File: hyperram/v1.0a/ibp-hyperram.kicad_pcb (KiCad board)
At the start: 2 copper layers, 18 x 42 mm, 6 parts, among them J2 PMOD, J4 PMOD, U1 S70KL1281

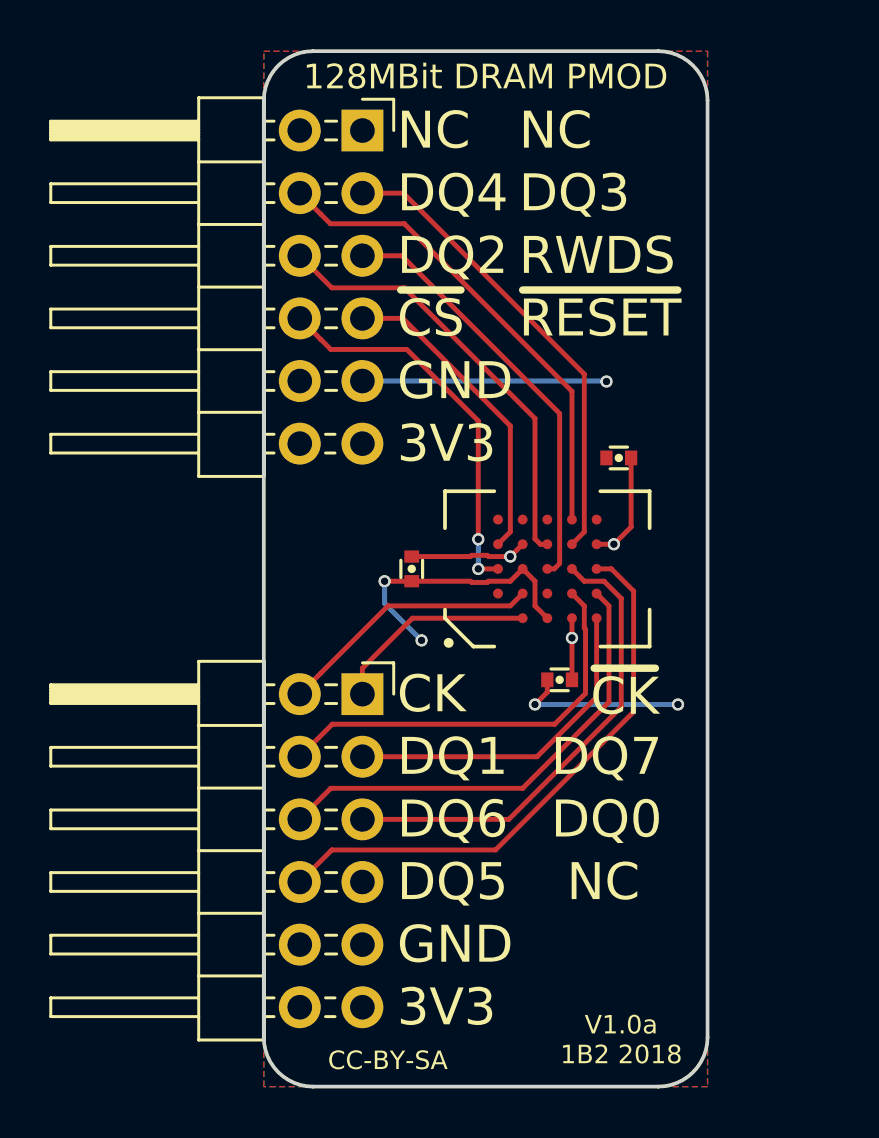
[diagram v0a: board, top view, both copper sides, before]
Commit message: Corrected silkscreen legend, roundrect pads.
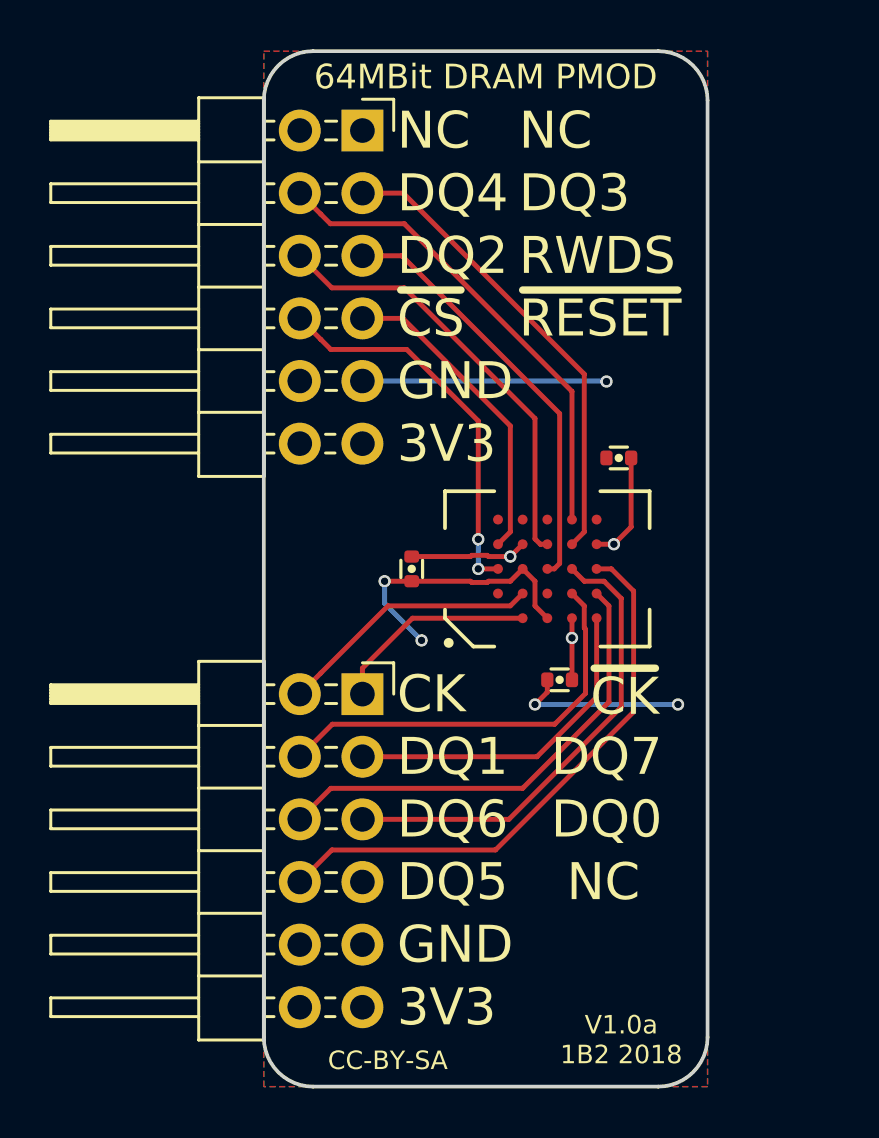
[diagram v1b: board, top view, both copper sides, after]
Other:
- board text added: "64MBit DRAM PMOD"
- board text removed: "128MBit DRAM PMOD"
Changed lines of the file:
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@@
-(kicad_pcb (version 20171130) (host pcbnew 5.0.0-rc2-dev-unknown-1ac905d~64~ubuntu16.04.1)
+(kicad_pcb (version 20171130) (host pcbnew 5.0.0-rc2-dev-unknown-5a90858~64~ubuntu16.04.1)
   (general
     (thickness 0.8)
@@
     (mod_text_size 1 1)
     (mod_text_width 0.15)
-    (pad_size 1.7 1.7)
-    (pad_drill 1)
+    (pad_size 0.5 0.6)
+    (pad_drill 0)
     (pad_to_mask_clearance 0.05)
     (aux_axis_origin 0 0)
@@
     (fp_line (start -0.35 -0.44) (end 0.35 -0.44) (layer F.SilkS) (width 0.13))
     (fp_line (start 0.35 0.44) (end -0.35 0.44) (layer F.SilkS) (width 0.13))
-    (pad 1 smd rect (at -0.5 0 180) (size 0.5 0.6) (layers F.Cu F.Paste F.Mask)
-      (net 3 +3V3))
-    (pad 2 smd rect (at 0.5 0 180) (size 0.5 0.6) (layers F.Cu F.Paste F.Mask)
+    (pad 1 smd roundrect (at -0.5 0 180) (size 0.5 0.6) (layers F.Cu F.Paste F.Mask) (roundrect_rratio 0.25)
+      (net 3 +3V3))
+    (pad 2 smd roundrect (at 0.5 0 180) (size 0.5 0.6) (layers F.Cu F.Paste F.Mask) (roundrect_rratio 0.25)
       (net 1 GND))
     (model ${KISYS3DMOD}/Capacitor_SMD.3dshapes/C_0402_1005Metric.step
@@
     (fp_line (start -0.95 -0.5) (end 0.95 -0.5) (layer F.CrtYd) (width 0.05))
     (fp_circle (center 0 0) (end 0 -0.085) (layer F.SilkS) (width 0.17))
-    (pad 2 smd rect (at 0.5 0 180) (size 0.5 0.6) (layers F.Cu F.Paste F.Mask)
-      (net 1 GND))
-    (pad 1 smd rect (at -0.5 0 180) (size 0.5 0.6) (layers F.Cu F.Paste F.Mask)
+    (pad 2 smd roundrect (at 0.5 0 180) (size 0.5 0.6) (layers F.Cu F.Paste F.Mask) (roundrect_rratio 0.25)
+      (net 1 GND))
+    (pad 1 smd roundrect (at -0.5 0 180) (size 0.5 0.6) (layers F.Cu F.Paste F.Mask) (roundrect_rratio 0.25)
       (net 3 +3V3))
     (model Capacitors_SMD.3dshapes/C_0402.wrl
@@
     (fp_line (start -0.35 -0.44) (end 0.35 -0.44) (layer F.SilkS) (width 0.13))
     (fp_line (start 0.35 0.44) (end -0.35 0.44) (layer F.SilkS) (width 0.13))
-    (pad 1 smd rect (at -0.5 0 270) (size 0.5 0.6) (layers F.Cu F.Paste F.Mask)
-      (net 3 +3V3))
-    (pad 2 smd rect (at 0.5 0 270) (size 0.5 0.6) (layers F.Cu F.Paste F.Mask)
+    (pad 1 smd roundrect (at -0.5 0 270) (size 0.5 0.6) (layers F.Cu F.Paste F.Mask) (roundrect_rratio 0.25)
+      (net 3 +3V3))
+    (pad 2 smd roundrect (at 0.5 0 270) (size 0.5 0.6) (layers F.Cu F.Paste F.Mask) (roundrect_rratio 0.25)
       (net 1 GND))
     (model ${KISYS3DMOD}/Capacitor_SMD.3dshapes/C_0402_1005Metric.step
@@
     (effects (font (size 0.75 0.75) (thickness 0.1875)) (justify mirror))
   )
-  (gr_text "128MBit DRAM PMOD" (at 49 24.045) (layer B.SilkS)
+  (gr_text "64MBit DRAM PMOD" (at 49 24.045) (layer B.SilkS)
     (effects (font (size 1 1) (thickness 0.25)) (justify mirror))
   )
-  (gr_text "128MBit DRAM PMOD" (at 49 24.045) (layer F.SilkS)
+  (gr_text "64MBit DRAM PMOD" (at 49 24.045) (layer F.SilkS)
     (effects (font (size 1 1) (thickness 0.25)))
   )

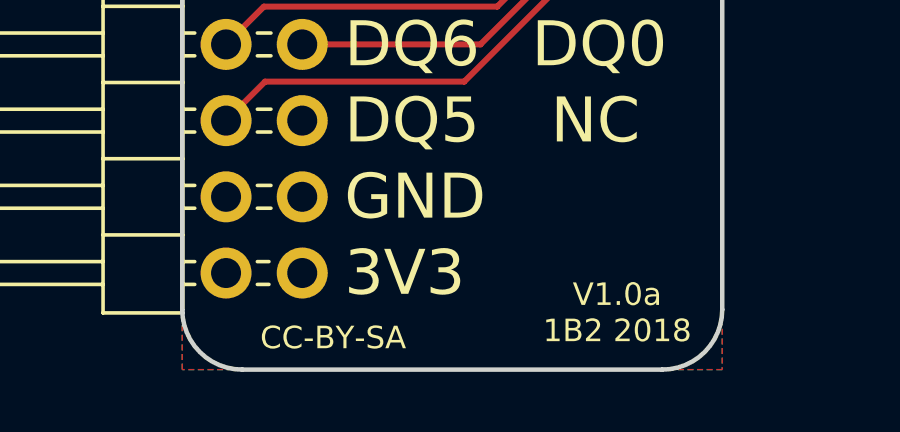
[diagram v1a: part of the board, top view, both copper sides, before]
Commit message: Spelled out 1BitSquared copyright.
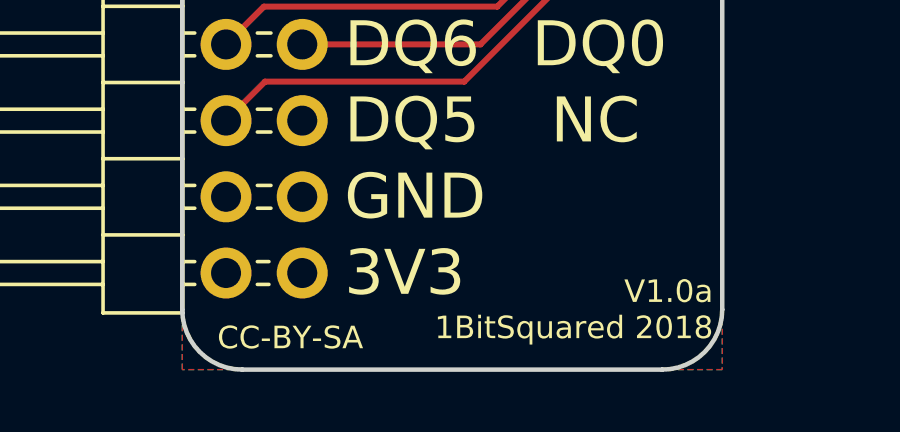
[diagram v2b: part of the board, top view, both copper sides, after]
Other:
- board text added: "V1.0a 1BitSquared 2018"
- board text removed: "V1.0a 1B2 2018"
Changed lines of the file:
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@@
-(kicad_pcb (version 20171130) (host pcbnew 5.0.0-rc2-dev-unknown-5a90858~64~ubuntu16.04.1)
+(kicad_pcb (version 20171130) (host pcbnew 5.0.0-fee4fd1~66~ubuntu18.04.1)
   (general
     (thickness 0.8)
@@
       (hpglpennumber 1)
       (hpglpenspeed 20)
-      (hpglpendiameter 15)
+      (hpglpendiameter 15.000000)
       (psnegative false)
       (psa4output false)
@@
       (drillshape 0)
       (scaleselection 1)
-      (outputdirectory gerber))
+      (outputdirectory "gerber"))
   )
   (net 0 "")
@@
     )
   )
+  (gr_text "V1.0a\n1BitSquared 2018" (at 57.6 63) (layer B.SilkS)
+    (effects (font (size 0.75 0.75) (thickness 0.1875)) (justify left mirror))
+  )
   (gr_text NC (at 52.285 56.7) (layer F.SilkS)
     (effects (font (size 1.5 1.5) (thickness 0.3)) (justify left))
@@
     (effects (font (size 1.5 1.5) (thickness 0.3)) (justify left))
   )
-  (gr_text CC-BY-SA (at 44.93 63.94) (layer B.SilkS)
+  (gr_text CC-BY-SA (at 43.8 63.94) (layer B.SilkS)
     (effects (font (size 0.75 0.75) (thickness 0.1875)) (justify mirror))
   )
-  (gr_text CC-BY-SA (at 45.03 63.94) (layer F.SilkS)
+  (gr_text CC-BY-SA (at 43.6 63.94) (layer F.SilkS)
     (effects (font (size 0.75 0.75) (thickness 0.1875)))
   )
-  (gr_text "V1.0a\n1B2 2018" (at 54.5 63.1) (layer F.SilkS)
-    (effects (font (size 0.75 0.75) (thickness 0.1875)))
-  )
-  (gr_text "V1.0a\n1B2 2018" (at 54.5 63.1) (layer B.SilkS)
-    (effects (font (size 0.75 0.75) (thickness 0.1875)) (justify mirror))
+  (gr_text "V1.0a\n1BitSquared 2018" (at 57.7 63) (layer F.SilkS)
+    (effects (font (size 0.75 0.75) (thickness 0.1875)) (justify right))
   )
   (gr_text "64MBit DRAM PMOD" (at 49 24.045) (layer B.SilkS)

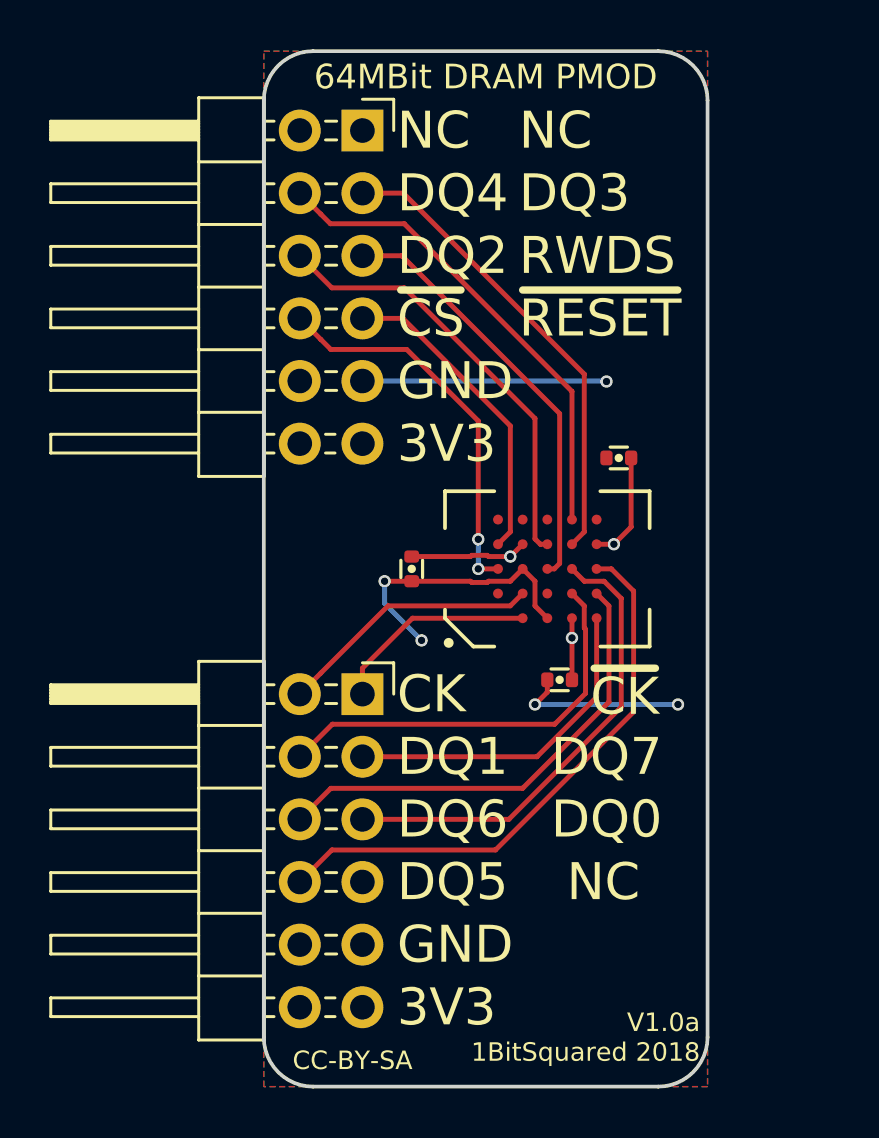
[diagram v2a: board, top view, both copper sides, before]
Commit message: Extended board outline to extend under the pin headers.
This makes assembly and alignment of the PMOD pin headers easier.
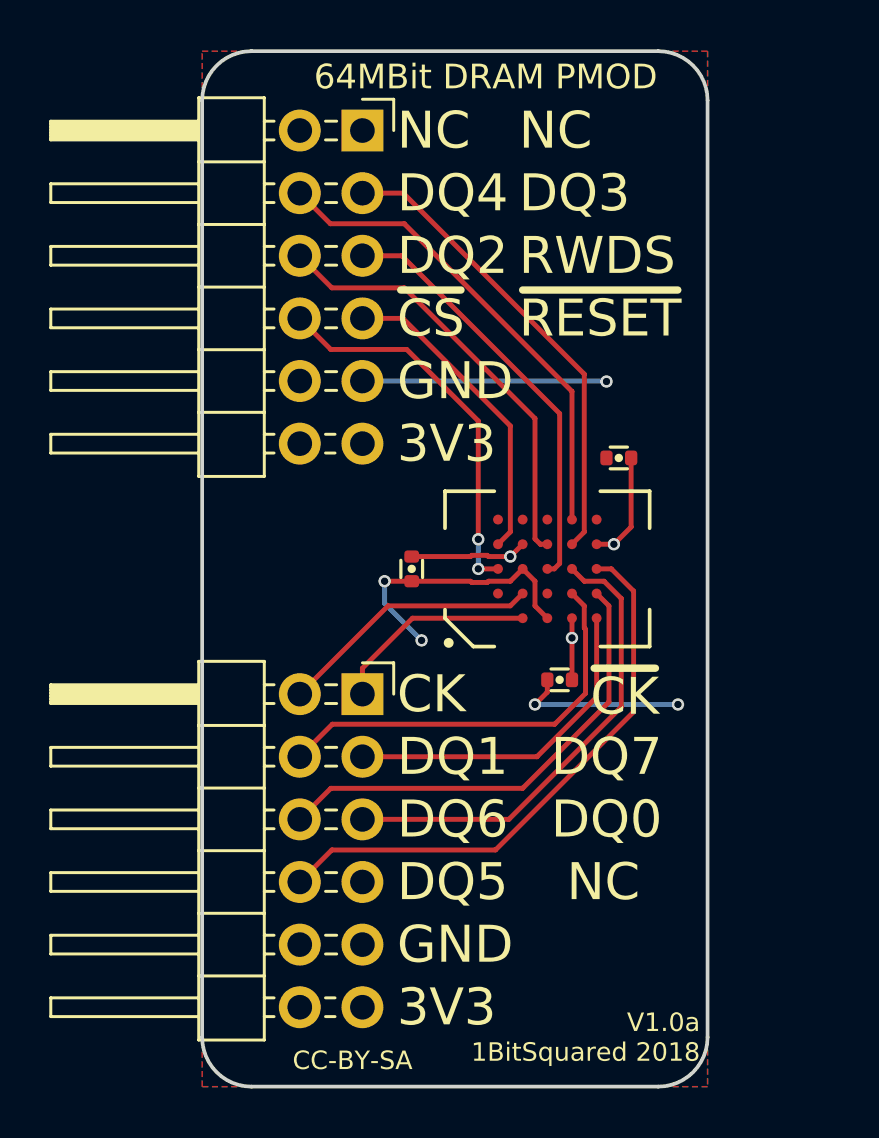
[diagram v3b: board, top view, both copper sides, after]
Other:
- board size 18 x 42 mm -> 20.5 x 42 mm
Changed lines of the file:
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@@
     (thickness 0.8)
     (drawings 54)
-    (tracks 105)
+    (tracks 102)
     (zones 0)
     (modules 6)
@@
   )
   (gr_arc (start 56 25) (end 58 25) (angle -90) (layer Edge.Cuts) (width 0.15))
-  (gr_arc (start 42 25) (end 42 23) (angle -90) (layer Edge.Cuts) (width 0.15))
-  (gr_arc (start 42 63) (end 40 63) (angle -90) (layer Edge.Cuts) (width 0.15))
+  (gr_arc (start 39.5 25) (end 39.5 23) (angle -90) (layer Edge.Cuts) (width 0.15))
+  (gr_arc (start 39.5 63) (end 37.5 63) (angle -90) (layer Edge.Cuts) (width 0.15))
   (gr_arc (start 56 63) (end 56 65) (angle -90) (layer Edge.Cuts) (width 0.15))
   (gr_line (start 58 25) (end 58 63) (layer Edge.Cuts) (width 0.15))
-  (gr_line (start 42 23) (end 56 23) (layer Edge.Cuts) (width 0.15))
-  (gr_line (start 40 63) (end 40 25) (layer Edge.Cuts) (width 0.15))
-  (gr_line (start 56 65) (end 42 65) (layer Edge.Cuts) (width 0.15))
+  (gr_line (start 39.5 23) (end 56 23) (layer Edge.Cuts) (width 0.15))
+  (gr_line (start 37.5 63) (end 37.5 25) (layer Edge.Cuts) (width 0.15))
+  (gr_line (start 56 65) (end 39.5 65) (layer Edge.Cuts) (width 0.15))
   (segment (start 51.5 46) (end 51 45.5) (width 0.2) (layer F.Cu) (net 1))
   (segment (start 51 44.5) (end 50.5 44) (width 0.2) (layer F.Cu) (net 1))
@@
   (segment (start 53.5 49.2) (end 53.5 46) (width 0.2) (layer F.Cu) (net 4))
   (segment (start 51.08 51.62) (end 53.5 49.2) (width 0.2) (layer F.Cu) (net 4))
-  (segment (start 42.309999 48.230001) (end 41.46 49.08) (width 0.2) (layer F.Cu) (net 6))
-  (segment (start 45.039999 45.500001) (end 42.309999 48.230001) (width 0.2) (layer F.Cu) (net 6))
-  (segment (start 49.999999 45.500001) (end 45.039999 45.500001) (width 0.2) (layer F.Cu) (net 6))
-  (segment (start 50.5 45) (end 49.999999 45.500001) (width 0.2) (layer F.Cu) (net 6))
+  (segment (start 49.999999 45.500001) (end 50.5 45) (width 0.2) (layer F.Cu) (net 6))
+  (segment (start 41.46 49.08) (end 45.039999 45.500001) (width 0.2) (layer F.Cu) (net 6))
+  (segment (start 45.039999 45.500001) (end 49.999999 45.500001) (width 0.2) (layer F.Cu) (net 6))
   (segment (start 53 45.5) (end 52.5 45) (width 0.2) (layer F.Cu) (net 8))
   (segment (start 53 46.4) (end 53 45.5) (width 0.2) (layer F.Cu) (net 8))
@@
   (via (at 48.7 42.8) (size 0.5) (drill 0.3) (layers F.Cu B.Cu) (net 10))
   (segment (start 48.7 44) (end 48.7 42.8) (width 0.2) (layer B.Cu) (net 10))
-  (segment (start 48.7 42.8) (end 48.7 38) (width 0.2) (layer F.Cu) (net 10))
-  (segment (start 42.309999 34.689999) (end 41.46 33.84) (width 0.2) (layer F.Cu) (net 10))
-  (segment (start 42.72 35.1) (end 42.309999 34.689999) (width 0.2) (layer F.Cu) (net 10))
-  (segment (start 48.7 38) (end 45.8 35.1) (width 0.2) (layer F.Cu) (net 10))
-  (segment (start 45.8 35.1) (end 42.72 35.1) (width 0.2) (layer F.Cu) (net 10))
+  (segment (start 48.7 38) (end 48.7 42.8) (width 0.2) (layer F.Cu) (net 10))
+  (segment (start 45.8 35.1) (end 48.7 38) (width 0.2) (layer F.Cu) (net 10))
+  (segment (start 41.46 33.84) (end 42.72 35.1) (width 0.2) (layer F.Cu) (net 10))
+  (segment (start 42.72 35.1) (end 45.8 35.1) (width 0.2) (layer F.Cu) (net 10))
   (segment (start 51.782842 44) (end 52 43.782842) (width 0.2) (layer F.Cu) (net 11))
   (segment (start 51.5 44) (end 51.782842 44) (width 0.2) (layer F.Cu) (net 11))
@@
   (segment (start 45.66 28.76) (end 44 28.76) (width 0.2) (layer F.Cu) (net 16))
   (segment (start 52.5 43) (end 53 42.5) (width 0.2) (layer F.Cu) (net 16))
-  (segment (start 42.309999 29.609999) (end 41.46 28.76) (width 0.2) (layer F.Cu) (net 20))
-  (segment (start 52.5 42) (end 52.5 36.8) (width 0.2) (layer F.Cu) (net 20))
-  (segment (start 52.5 36.8) (end 45.7 30) (width 0.2) (layer F.Cu) (net 20))
-  (segment (start 45.7 30) (end 42.7 30) (width 0.2) (layer F.Cu) (net 20))
-  (segment (start 42.7 30) (end 42.309999 29.609999) (width 0.2) (layer F.Cu) (net 20))
+  (segment (start 52.5 36.8) (end 52.5 42) (width 0.2) (layer F.Cu) (net 20))
+  (segment (start 45.7 30) (end 52.5 36.8) (width 0.2) (layer F.Cu) (net 20))
+  (segment (start 41.46 28.76) (end 42.7 30) (width 0.2) (layer F.Cu) (net 20))
+  (segment (start 42.7 30) (end 45.7 30) (width 0.2) (layer F.Cu) (net 20))
   (zone (net 1) (net_name GND) (layer F.Cu) (hatch edge 0.508)
     (connect_pads (clearance 0.25))
@@
     (polygon
       (pts
-        (xy 58 64.999999) (xy 39.999999 65) (xy 39.999999 23) (xy 58 23.000001)
+        (xy 58 64.999999) (xy 37.5 65) (xy 37.5 23) (xy 58 23.000001)
       )
     )
@@
     (polygon
       (pts
-        (xy 58 64.999999) (xy 39.999999 65) (xy 39.999999 23) (xy 58 23.000001)
+        (xy 58 64.999999) (xy 37.5 65) (xy 37.5 23) (xy 58 23.000001)
       )
     )

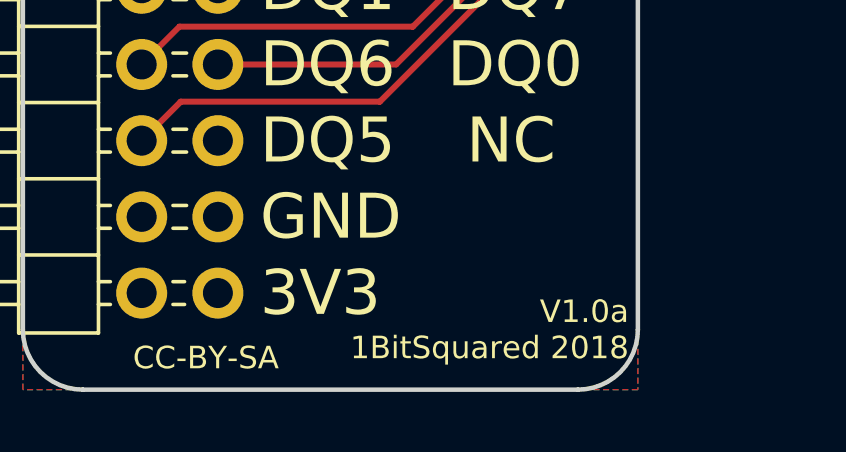
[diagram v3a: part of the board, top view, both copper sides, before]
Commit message: One more adjustment to the (C) block.
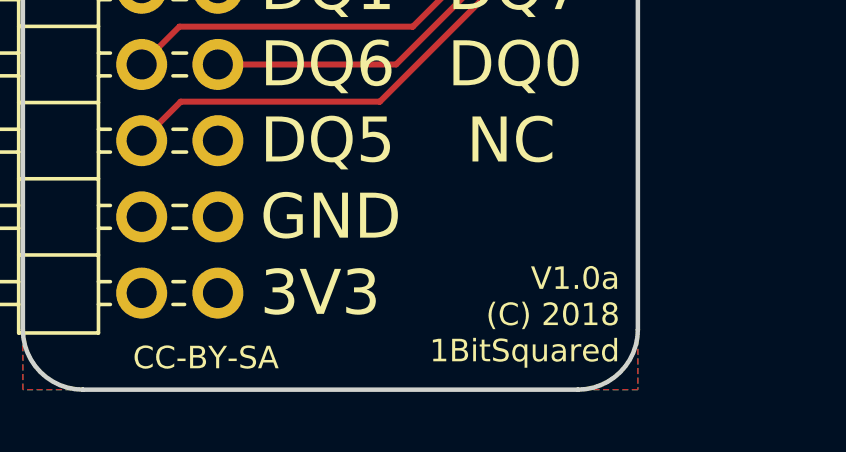
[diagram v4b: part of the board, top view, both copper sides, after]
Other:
- board text added: "V1.0a (C) 2018 1BitSquared"
- board text removed: "V1.0a 1BitSquared 2018"
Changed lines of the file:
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@@
     )
   )
-  (gr_text "V1.0a\n1BitSquared 2018" (at 57.6 63) (layer B.SilkS)
+  (gr_text "V1.0a\n(C) 2018\n1BitSquared" (at 57.4 62.5) (layer B.SilkS)
     (effects (font (size 0.75 0.75) (thickness 0.1875)) (justify left mirror))
   )
@@
     (effects (font (size 0.75 0.75) (thickness 0.1875)))
   )
-  (gr_text "V1.0a\n1BitSquared 2018" (at 57.7 63) (layer F.SilkS)
+  (gr_text "V1.0a\n(C) 2018\n1BitSquared" (at 57.4 62.5) (layer F.SilkS)
     (effects (font (size 0.75 0.75) (thickness 0.1875)) (justify right))
   )
